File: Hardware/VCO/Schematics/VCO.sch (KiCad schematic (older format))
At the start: 25 parts, among them J1 Conn_01x02, J2 Conn_01x02, J3 Conn_01x02

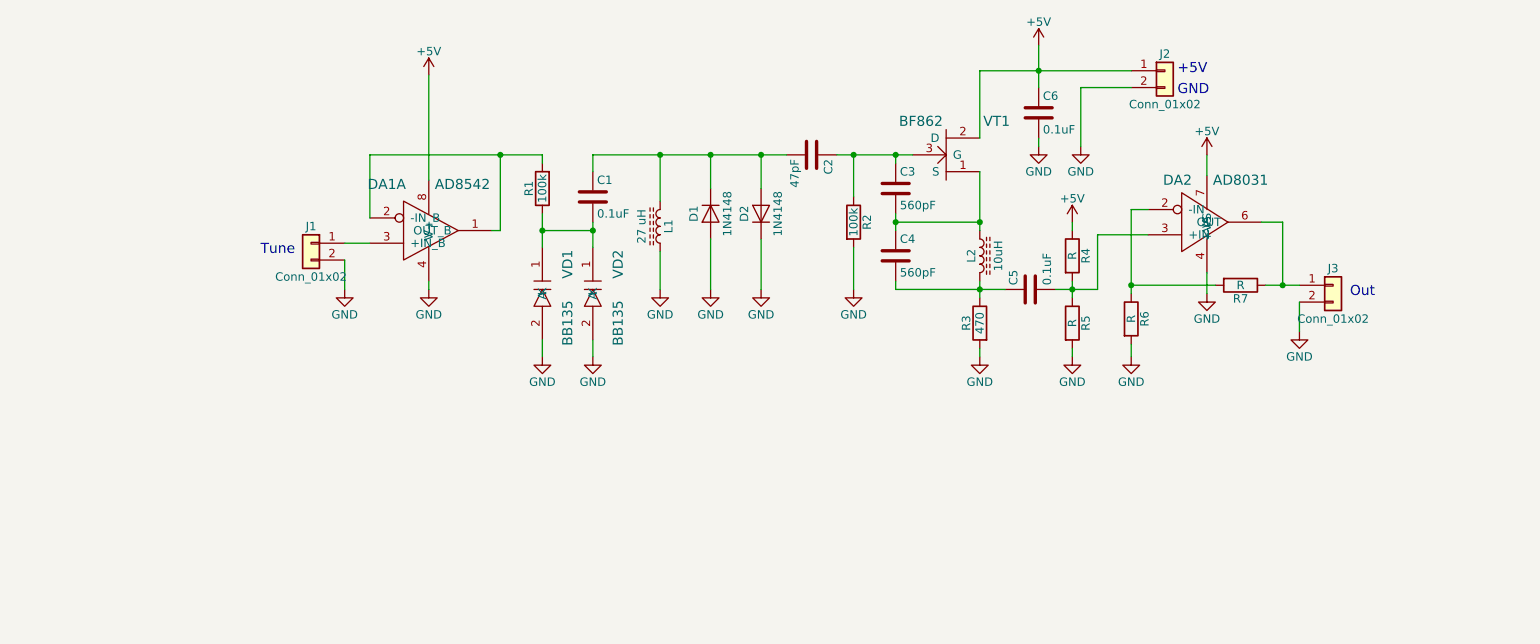
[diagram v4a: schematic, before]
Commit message: - Hope that variant of VCO out amplifier will work (will check it tomorrow).
- Some simulations (QUCS is good, but still fail to simulate my schemes properly).
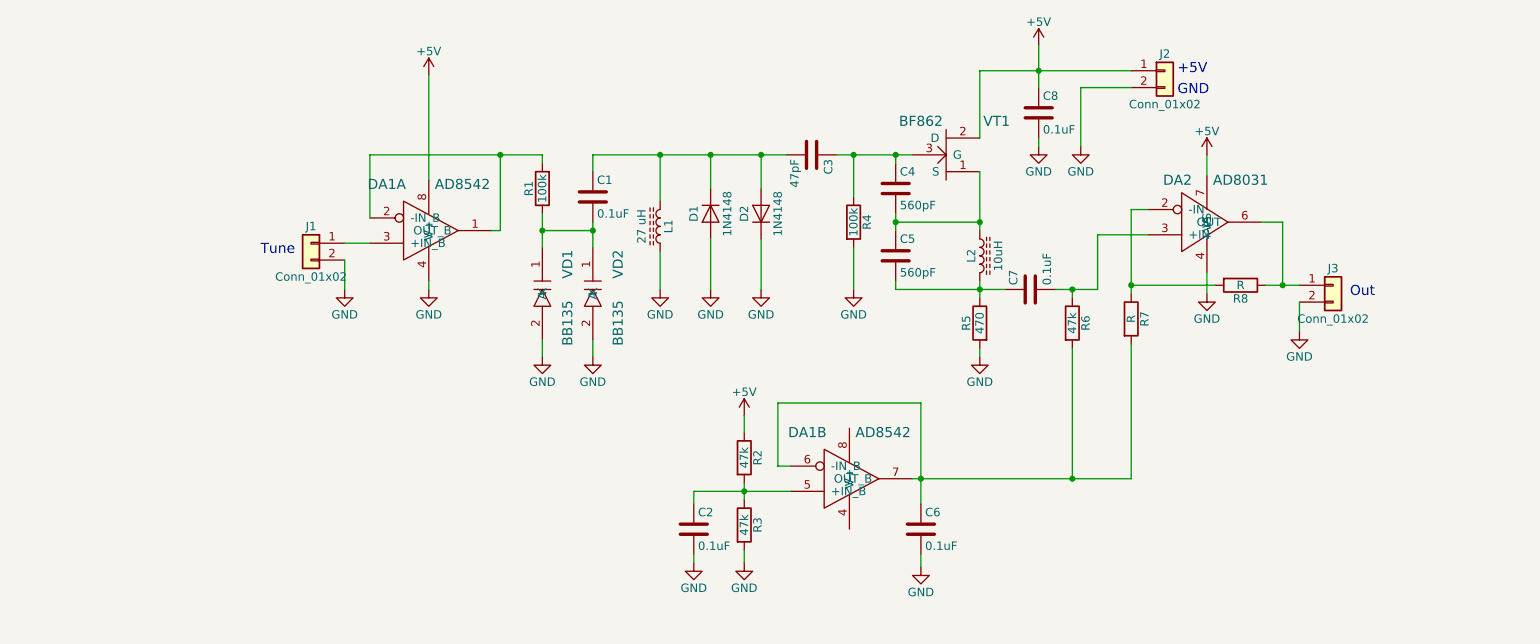
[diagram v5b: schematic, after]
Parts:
- removed R4: R, symbol R
- added C2, C6: 0.1uF, symbol C
- added unit 2 of DA1
- added R2, R3: 47k, symbol R
- R6: renamed from R5; value R -> 47k
- renumbered C2 to C3, C3 to C4, C4 to C5, C5 to C7, C6 to C8, R2 to R4, R3 to R5, R6 to R7, R7 to R8
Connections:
- net +5V: now also R2.1
- net GND: now also C2.2, C6.2, R3.2; no longer R6.2, R7.2
- new net: C6.1, DA1.6 (-IN_B), DA1.7 (OUT_B), R6.2, R7.2
- new net: C2.1, DA1.5 (+IN_B), R2.2, R3.1
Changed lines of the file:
@@
 GND
 $Comp
-L GND #PWR16
+L GND #PWR17
 U 1 1 5B706542
 P 8100 1500
-F 0 "#PWR16" H 8100 1250 50  0001 C CNN
+F 0 "#PWR17" H 8100 1250 50  0001 C CNN
 F 1 "GND" H 8100 1350 50  0000 C CNN
 F 2 "" H 8100 1500 50  0001 C CNN
@@
 $EndComp
 $Comp
-L C C6
+L C C8
 U 1 1 5B70657A
 P 7850 1300
-F 0 "C6" H 7875 1400 50  0000 L CNN
+F 0 "C8" H 7875 1400 50  0000 L CNN
 F 1 "0.1uF" H 7875 1200 50  0000 L CNN
 F 2 "" H 7888 1150 50  0001 C CNN
@@
 $EndComp
 $Comp
-L GND #PWR13
+L GND #PWR16
 U 1 1 5B706662
 P 7850 1500
-F 0 "#PWR13" H 7850 1250 50  0001 C CNN
+F 0 "#PWR16" H 7850 1250 50  0001 C CNN
 F 1 "GND" H 7850 1350 50  0000 C CNN
 F 2 "" H 7850 1500 50  0001 C CNN
@@
 $EndComp
 $Comp
-L GND #PWR11
+L GND #PWR14
 U 1 1 5B7069A3
 P 7500 2750
-F 0 "#PWR11" H 7500 2500 50  0001 C CNN
+F 0 "#PWR14" H 7500 2500 50  0001 C CNN
 F 1 "GND" H 7500 2600 50  0000 C CNN
 F 2 "" H 7500 2750 50  0001 C CNN
@@
 $EndComp
 $Comp
-L C C3
+L C C4
 U 1 1 5B706A22
 P 7000 1750
-F 0 "C3" H 7025 1850 50  0000 L CNN
+F 0 "C4" H 7025 1850 50  0000 L CNN
 F 1 "560pF" H 7025 1650 50  0000 L CNN
 F 2 "" H 7038 1600 50  0001 C CNN
@@
 $EndComp
 $Comp
-L C C4
+L C C5
 U 1 1 5B706AA9
 P 7000 2150
-F 0 "C4" H 7025 2250 50  0000 L CNN
+F 0 "C5" H 7025 2250 50  0000 L CNN
 F 1 "560pF" H 7025 2050 50  0000 L CNN
 F 2 "" H 7038 2000 50  0001 C CNN
@@
 $EndComp
 $Comp
-L R R2
+L R R4
 U 1 1 5B706C78
 P 6750 1950
-F 0 "R2" V 6830 1950 50  0000 C CNN
+F 0 "R4" V 6830 1950 50  0000 C CNN
 F 1 "100k" V 6750 1950 50  0000 C CNN
 F 2 "" V 6680 1950 50  0001 C CNN
@@
 $EndComp
 $Comp
-L GND #PWR9
+L GND #PWR12
 U 1 1 5B706D03
 P 6750 2350
-F 0 "#PWR9" H 6750 2100 50  0001 C CNN
+F 0 "#PWR12" H 6750 2100 50  0001 C CNN
 F 1 "GND" H 6750 2200 50  0000 C CNN
 F 2 "" H 6750 2350 50  0001 C CNN
@@
 $EndComp
 $Comp
-L C C2
+L C C3
 U 1 1 5B707492
 P 6500 1550
-F 0 "C2" H 6525 1650 50  0000 L CNN
+F 0 "C3" H 6525 1650 50  0000 L CNN
 F 1 "47pF" H 6525 1450 50  0000 L CNN
 F 2 "" H 6538 1400 50  0001 C CNN
@@
 $EndComp
 $Comp
-L GND #PWR8
+L GND #PWR11
 U 1 1 5B707677
 P 6200 2350
-F 0 "#PWR8" H 6200 2100 50  0001 C CNN
+F 0 "#PWR11" H 6200 2100 50  0001 C CNN
 F 1 "GND" H 6200 2200 50  0000 C CNN
 F 2 "" H 6200 2350 50  0001 C CNN
@@
 $EndComp
 $Comp
-L +5V #PWR12
+L +5V #PWR15
 U 1 1 5B720252
 P 7850 900
-F 0 "#PWR12" H 7850 750 50  0001 C CNN
+F 0 "#PWR15" H 7850 750 50  0001 C CNN
 F 1 "+5V" H 7850 1040 50  0000 C CNN
 F 2 "" H 7850 900 50  0001 C CNN
@@
 $EndComp
 $Comp
-L R R6
+L R R7
 U 1 1 5B7264A0
 P 8400 2525
-F 0 "R6" V 8480 2525 50  0000 C CNN
+F 0 "R7" V 8480 2525 50  0000 C CNN
 F 1 "R" V 8400 2525 50  0000 C CNN
 F 2 "" V 8330 2525 50  0001 C CNN
@@
 $EndComp
 $Comp
-L R R7
+L R R8
 U 1 1 5B7266B2
 P 9050 2325
-F 0 "R7" V 9130 2325 50  0000 C CNN
+F 0 "R8" V 9130 2325 50  0000 C CNN
 F 1 "R" V 9050 2325 50  0000 C CNN
 F 2 "" V 8980 2325 50  0001 C CNN
@@
 	1    9050 2325
 	0    1    1    0
-$EndComp
-$Comp
-L GND #PWR17
-U 1 1 5B7269A1
-P 8400 2750
-F 0 "#PWR17" H 8400 2500 50  0001 C CNN
-F 1 "GND" H 8400 2600 50  0000 C CNN
-F 2 "" H 8400 2750 50  0001 C CNN
-F 3 "" H 8400 2750 50  0001 C CNN
-	1    8400 2750
-	1    0    0    -1
 $EndComp
 $Comp
@@
 $EndComp
 $Comp
-L GND #PWR7
+L GND #PWR8
 U 1 1 5B789BB4
 P 5900 2350
-F 0 "#PWR7" H 5900 2100 50  0001 C CNN
+F 0 "#PWR8" H 5900 2100 50  0001 C CNN
 F 1 "GND" H 5900 2200 50  0000 C CNN
 F 2 "" H 5900 2350 50  0001 C CNN
@@
 $EndComp
 $Comp
-L R R3
+L R R5
 U 1 1 5B78B0BF
 P 7500 2550
-F 0 "R3" V 7580 2550 50  0000 C CNN
+F 0 "R5" V 7580 2550 50  0000 C CNN
 F 1 "470" V 7500 2550 50  0000 C CNN
 F 2 "" V 7430 2550 50  0001 C CNN
@@
 $EndComp
 $Comp
-L C C5
+L C C7
 U 1 1 5B78B2F8
 P 7800 2350
-F 0 "C5" H 7825 2450 50  0000 L CNN
+F 0 "C7" H 7825 2450 50  0000 L CNN
 F 1 "0.1uF" H 7825 2250 50  0000 L CNN
 F 2 "" H 7838 2200 50  0001 C CNN
@@
 $EndComp
 $Comp
-L R R4
-U 1 1 5B78B62C
-P 8050 2150
-F 0 "R4" V 8130 2150 50  0000 C CNN
-F 1 "R" V 8050 2150 50  0000 C CNN
-F 2 "" V 7980 2150 50  0001 C CNN
-F 3 "" H 8050 2150 50  0001 C CNN
-	1    8050 2150
-	1    0    0    -1
-$EndComp
-$Comp
-L R R5
+L R R6
 U 1 1 5B78B691
 P 8050 2550
-F 0 "R5" V 8130 2550 50  0000 C CNN
-F 1 "R" V 8050 2550 50  0000 C CNN
+F 0 "R6" V 8130 2550 50  0000 C CNN
+F 1 "47k" V 8050 2550 50  0000 C CNN
 F 2 "" V 7980 2550 50  0001 C CNN
 F 3 "" H 8050 2550 50  0001 C CNN
@@
 	1    0    0    -1
 $EndComp
-$Comp
-L GND #PWR15
-U 1 1 5B78B6E4
-P 8050 2750
-F 0 "#PWR15" H 8050 2500 50  0001 C CNN
-F 1 "GND" H 8050 2600 50  0000 C CNN
-F 2 "" H 8050 2750 50  0001 C CNN
-F 3 "" H 8050 2750 50  0001 C CNN
-	1    8050 2750
-	1    0    0    -1
-$EndComp
-$Comp
-L +5V #PWR14
-U 1 1 5B78B8F8
-P 8050 1950
-F 0 "#PWR14" H 8050 1800 50  0001 C CNN
-F 1 "+5V" H 8050 2090 50  0000 C CNN
-F 2 "" H 8050 1950 50  0001 C CNN
-F 3 "" H 8050 1950 50  0001 C CNN
-	1    8050 1950
-	1    0    0    -1
-$EndComp
 Wire Wire Line
 	7500 1050 8400 1050
@@
 	8900 2325 8400 2325
 Connection ~ 8400 2325
-Wire Wire Line
-	8400 2750 8400 2675
 Connection ~ 9300 2325
 Wire Wire Line
@@
 Wire Wire Line
 	7000 2350 7650 2350
-Wire Wire Line
-	8050 2300 8050 2400
 Connection ~ 8050 2350
-Wire Wire Line
-	8050 2750 8050 2700
-Wire Wire Line
-	8050 1950 8050 2000
 Wire Wire Line
 	8200 2025 8200 2350
@@
 Wire Wire Line
 	7000 2300 7000 2350
+Wire Wire Line
+	8050 2400 8050 2350
+$Comp
+L AD8542 DA1
+U 2 1 5B789D7D
+P 6700 3475
+F 0 "DA1" H 6475 3750 60  0000 C CNN
+F 1 "AD8542" H 6925 3750 60  0000 C CNN
+F 2 "" H 6725 3825 60  0001 C CNN
+F 3 "" H 6725 3825 60  0001 C CNN
+	2    6700 3475
+	1    0    0    -1
+$EndComp
+$Comp
+L R R2
+U 1 1 5B789E6A
+P 6100 3350
+F 0 "R2" V 6180 3350 50  0000 C CNN
+F 1 "47k" V 6100 3350 50  0000 C CNN
+F 2 "" V 6030 3350 50  0001 C CNN
+F 3 "" H 6100 3350 50  0001 C CNN
+	1    6100 3350
+	1    0    0    -1
+$EndComp
+$Comp
+L R R3
+U 1 1 5B789F61
+P 6100 3750
+F 0 "R3" V 6180 3750 50  0000 C CNN
+F 1 "47k" V 6100 3750 50  0000 C CNN
+F 2 "" V 6030 3750 50  0001 C CNN
+F 3 "" H 6100 3750 50  0001 C CNN
+	1    6100 3750
+	1    0    0    -1
+$EndComp
+Wire Wire Line
+	6375 3400 6300 3400
+Wire Wire Line
+	6300 3400 6300 3025
+Wire Wire Line
+	6300 3025 7150 3025
+Wire Wire Line
+	7150 3025 7150 3625
+Wire Wire Line
+	7100 3475 8400 3475
+Wire Wire Line
+	6100 3600 6100 3500
+Wire Wire Line
+	5800 3550 6375 3550
+Connection ~ 6100 3550
+$Comp
+L GND #PWR10
+U 1 1 5B78A2C6
+P 6100 3975
+F 0 "#PWR10" H 6100 3725 50  0001 C CNN
+F 1 "GND" H 6100 3825 50  0000 C CNN
+F 2 "" H 6100 3975 50  0001 C CNN
+F 3 "" H 6100 3975 50  0001 C CNN
+	1    6100 3975
+	1    0    0    -1
+$EndComp
+Wire Wire Line
+	6100 3975 6100 3900
+$Comp
+L +5V #PWR9
+U 1 1 5B78A378
+P 6100 3100
+F 0 "#PWR9" H 6100 2950 50  0001 C CNN
+F 1 "+5V" H 6100 3240 50  0000 C CNN
+F 2 "" H 6100 3100 50  0001 C CNN
+F 3 "" H 6100 3100 50  0001 C CNN
+	1    6100 3100
+	1    0    0    -1
+$EndComp
+Wire Wire Line
+	6100 3200 6100 3100
+$Comp
+L C C2
+U 1 1 5B78A998
+P 5800 3775
+F 0 "C2" H 5825 3875 50  0000 L CNN
+F 1 "0.1uF" H 5825 3675 50  0000 L CNN
+F 2 "" H 5838 3625 50  0001 C CNN
+F 3 "" H 5800 3775 50  0001 C CNN
+	1    5800 3775
+	1    0    0    -1
+$EndComp
+$Comp
+L GND #PWR7
+U 1 1 5B78AA1B
+P 5800 3975
+F 0 "#PWR7" H 5800 3725 50  0001 C CNN
+F 1 "GND" H 5800 3825 50  0000 C CNN
+F 2 "" H 5800 3975 50  0001 C CNN
+F 3 "" H 5800 3975 50  0001 C CNN
+	1    5800 3975
+	1    0    0    -1
+$EndComp
+Wire Wire Line
+	5800 3975 5800 3925
+Wire Wire Line
+	5800 3625 5800 3550
+Wire Wire Line
+	8050 3475 8050 2700
+Connection ~ 7150 3475
+Wire Wire Line
+	8400 3475 8400 2675
+Connection ~ 8050 3475
+$Comp
+L C C6
+U 1 1 5B78B961
+P 7150 3775
+F 0 "C6" H 7175 3875 50  0000 L CNN
+F 1 "0.1uF" H 7175 3675 50  0000 L CNN
+F 2 "" H 7188 3625 50  0001 C CNN
+F 3 "" H 7150 3775 50  0001 C CNN
+	1    7150 3775
+	1    0    0    -1
+$EndComp
+$Comp
+L GND #PWR13
+U 1 1 5B78B9B8
+P 7150 4000
+F 0 "#PWR13" H 7150 3750 50  0001 C CNN
+F 1 "GND" H 7150 3850 50  0000 C CNN
+F 2 "" H 7150 4000 50  0001 C CNN
+F 3 "" H 7150 4000 50  0001 C CNN
+	1    7150 4000
+	1    0    0    -1
+$EndComp
+Wire Wire Line
+	7150 4000 7150 3925
 $EndSCHEMATC

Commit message: Added current project status
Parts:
- R7: value R -> 4.7k
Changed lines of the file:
@@
 P 8400 2525
 F 0 "R7" V 8480 2525 50  0000 C CNN
-F 1 "R" V 8400 2525 50  0000 C CNN
+F 1 "4.7k" V 8400 2525 50  0000 C CNN
 F 2 "" V 8330 2525 50  0001 C CNN
 F 3 "" H 8400 2525 50  0001 C CNN

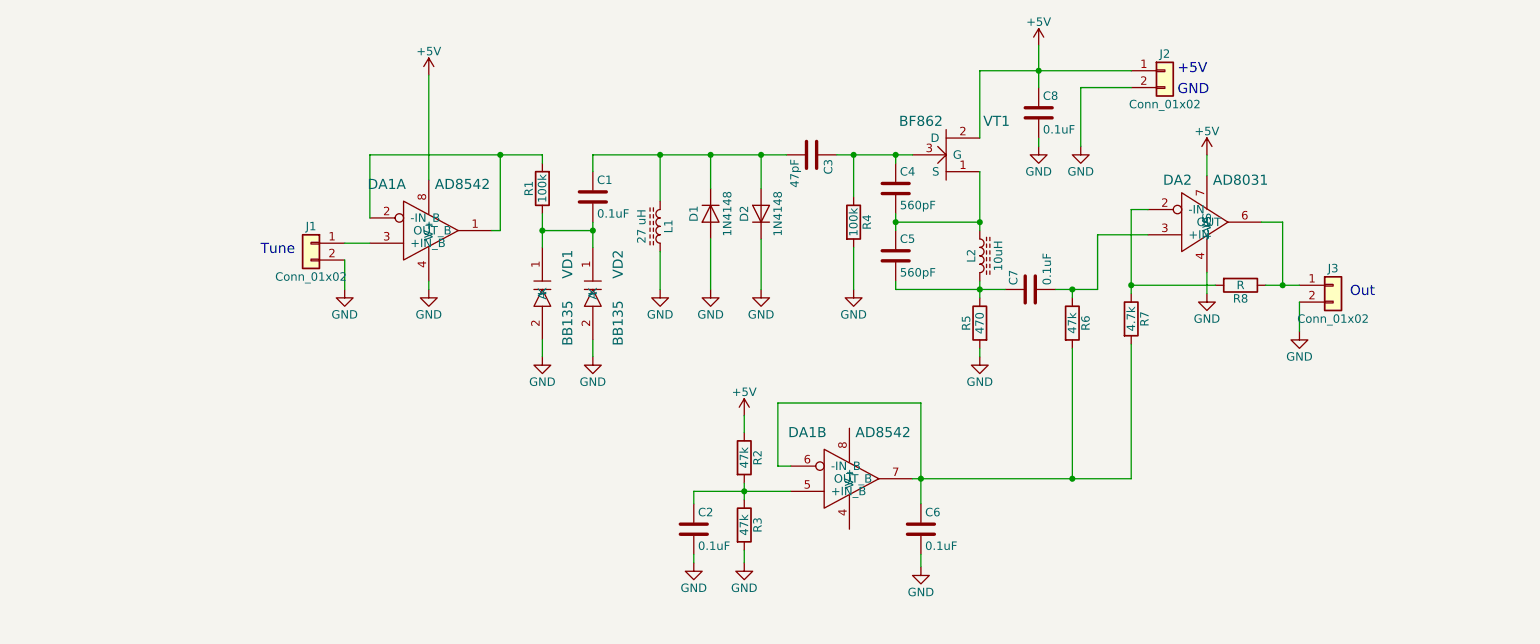
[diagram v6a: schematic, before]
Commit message: - Added BOM
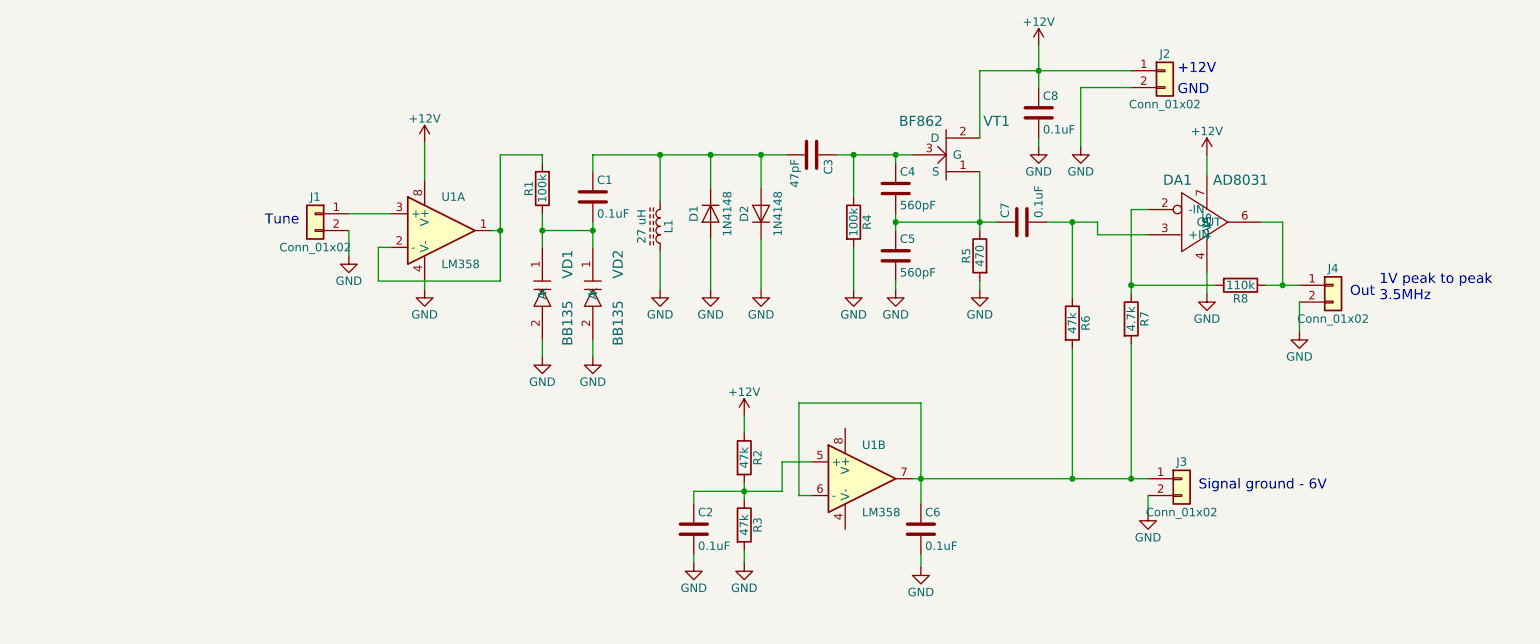
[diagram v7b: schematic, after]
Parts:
- removed DA1: AD8542, symbol AD8542
- removed L2: 10uH, symbol L_Core_Ferrite
- added J3: Conn_01x02, symbol Conn_01x02
- added U1: LM358, symbol LM358
- R8: value R -> 110k
- renumbered DA2 to DA1, J3 to J4
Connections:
- net GND: now also C5.2, J3.2 (Pin_2), U1.4 (V-)
- net at C4.2, C5.1, VT1.1 (S): now also C7.1, R5.1
- net at R1.2: now also U1.1, U1.2 (-)
- net at J1.1 (Pin_1): now also U1.3 (+)
- net at C6.1, R6.2, R7.2: now also J3.1 (Pin_1), U1.6 (-), U1.7
- net at C2.1, R2.2, R3.1: now also U1.5 (+)
- net +5V renamed +12V
- net +12V: now also U1.8 (V+)
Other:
- note added: "+12V"
- note added: "1V peak to peak\n3.5MHz"
- note added: "Signal ground - 6V"
- note removed: "+5V"
- moved on the sheet: C7, J1, R5
